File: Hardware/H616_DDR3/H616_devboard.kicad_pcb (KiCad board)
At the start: 8 copper layers, 50 x 50 mm, 169 parts, among them J1 Micro_SD_Card_Det2, J2 HDMI_D_1.4, J3 USB_C_Receptacle_USB2.0, J4 USB_C_Receptacle_USB2.0, J5 Conn_01x40_Pin, Q1 AO3420_C358680, Q2 AO3401A, Q3 AO3401A, SW1 CK_KMS2xxG, U1 H616, U10 D3V3XA4B10LP, U11 D3V3XA4B10LP, U2 K4B8G1646D, U3 AXP305, U4 SW6206, U6 KLMBG2JETD-B041, U7 AP6256, U8 D3V3XA4B10LP, U9 D3V3XA4B10LP, Y1 24MHz

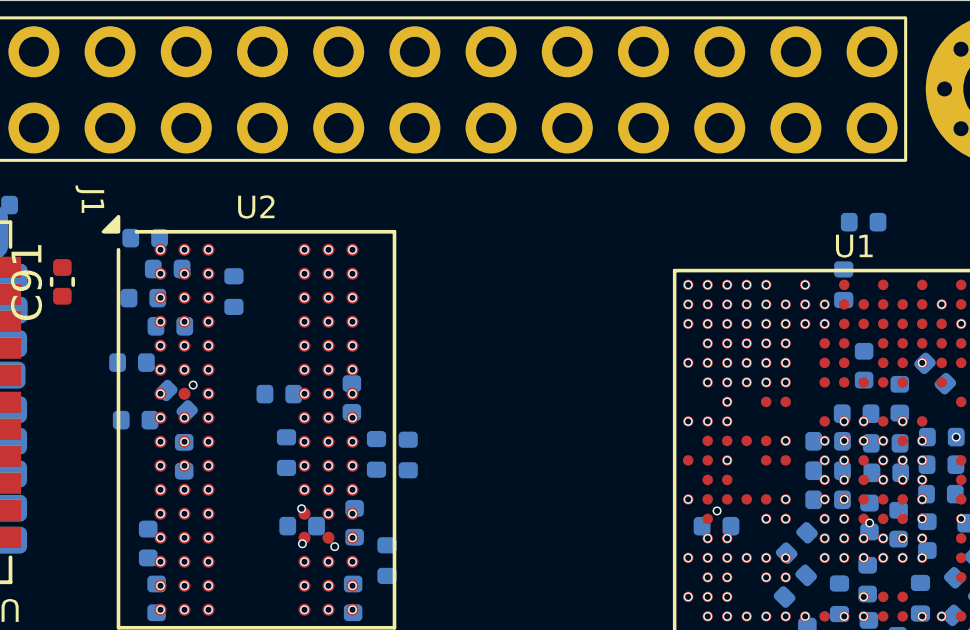
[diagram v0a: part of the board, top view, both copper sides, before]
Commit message: ddr3 trace
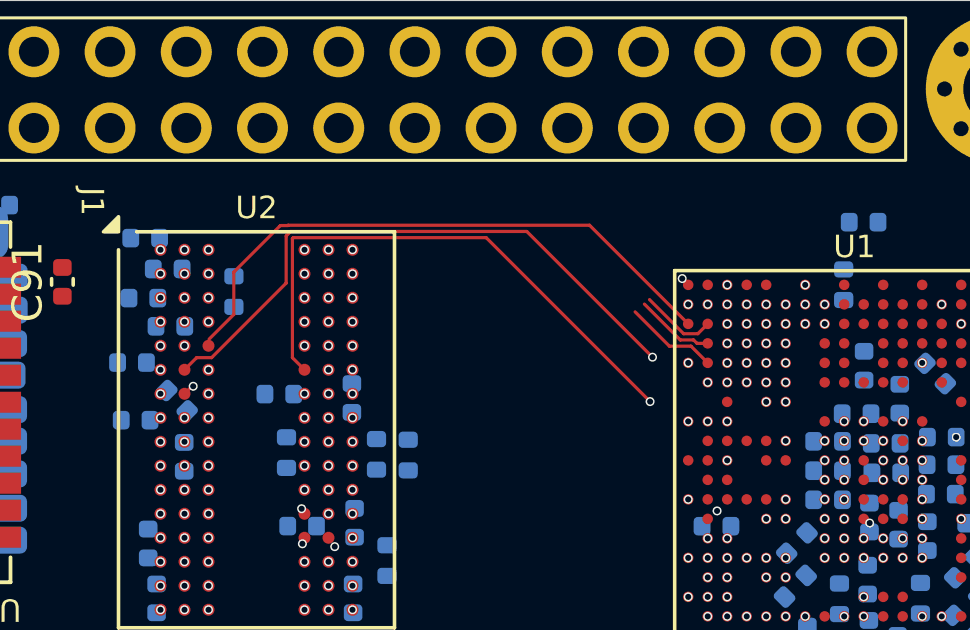
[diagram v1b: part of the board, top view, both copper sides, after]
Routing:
- net /DRAM/DQ1: track 0.00 -> 24.1 mm
- net /DRAM/DQ2: track 0.00 -> 20.2 mm
- net /DRAM/DQ0: track 0.00 -> 19.7 mm, vias 2 -> 0
- net /DRAM/SDQ21: track 0.00 -> 3.12 mm, vias 1 -> 0
- net /DRAM/SDQS1P: track 0.00 -> 2.92 mm
- net /DRAM/DQ10: track 0.00 -> 2.65 mm, vias 2 -> 1
- net /DRAM/DQ14: track 0.00 -> 2.55 mm, vias 2 -> 1
- net /DRAM/SDQS1N: track 0.00 -> 2.29 mm
- net /DRAM/DQ6: track 0.00 -> 0.39 mm, vias 1 -> 2
- net /DRAM/SDQ25: vias 0 -> 1
- net GND: vias 85 -> 84
- net /DRAM/SDQS0N: vias 2 -> 1
- net /DRAM/SDQM0: vias 2 -> 1
- net /DRAM/SDQ26: vias 0 -> 1
- net /DRAM/SDQ22: vias 1 -> 0
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
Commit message: ddr3 trace
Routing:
- removed copper zone on In3.Cu, net /POWER/VDD_CPU
- removed copper zone on In3.Cu, net /POWER/VDD_GPU
- removed copper zone on In1.Cu, net GND
- removed copper zone on In4.Cu, net GND
- removed copper zone on In6.Cu, net GND
- removed copper zone on In3.Cu, net VCC_DRAM
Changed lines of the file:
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@@
 		(net "Net-(U2-ZQ1)")
-	)
-	(zone
-		(net "GND")
-		(layers "In1.Cu" "In4.Cu" "In6.Cu")
-		(name "gnd_1")
-		(hatch edge 0.5)
-		(connect_pads yes
-			(clearance 0.254)
-		)
-		(min_thickness 0.25)
-		(fill yes
-			(thermal_gap 0.5)
-			(thermal_bridge_width 0.5)
-			(island_removal_mode 0)
-		)
-		(polygon
-			(pts
-				(xy 65.2 38.7) (xy 134.075 38.7) (xy 134.075 94.75) (xy 128.95 99.875) (xy 68.875 99.875) (xy 68.875 100)
-				(xy 65.2 96.325)
-			)
-		)
-	)
-	(zone
-		(net "/POWER/VDD_GPU")
-		(layer "In3.Cu")
-		(name "GPU")
-		(hatch edge 0.5)
-		(priority 2)
-		(connect_pads yes
-			(clearance 0.08)
-		)
-		(min_thickness 0.1)
-		(fill yes
-			(thermal_gap 0.5)
-			(thermal_bridge_width 0.5)
-			(smoothing fillet)
-			(radius 1)
-			(island_removal_mode 0)
-		)
-		(polygon
-			(pts
-				(xy 92.43 66.52) (xy 91.01 60.27) (xy 86.9 60.25) (xy 87.53 71.83) (xy 94.48 73.05) (xy 96.676125 77.316131)
-				(xy 106.537905 81.022909) (xy 107.441923 79.49738) (xy 110.264656 79.49199) (xy 110.69 77.55) (xy 107.881031 77.484421)
-				(xy 105.040094 70.498346) (xy 98.53202 68.529472) (xy 95.851615 69.229579) (xy 93.156219 68.375893)
-			)
-		)
-	)
-	(zone
-		(net "VCC_DRAM")
-		(layer "In3.Cu")
-		(name "DRAM")
-		(hatch edge 0.5)
-		(priority 1)
-		(connect_pads yes
-			(clearance 0.15)
-		)
-		(min_thickness 0.25)
-		(fill yes
-			(thermal_gap 0.5)
-			(thermal_bridge_width 0.5)
-			(smoothing fillet)
-			(radius 1)
-			(island_removal_mode 0)
-		)
-		(polygon
-			(pts
-				(xy 98.275 53.325) (xy 115.775 53.325) (xy 116.875 54.425) (xy 116.875 61.850274) (xy 112.73 63.05)
-				(xy 109.116 75.321741) (xy 107.478669 76.091362) (xy 106.77 73.8) (xy 106.860142 70.304477) (xy 104.55419 69.012348)
-				(xy 98.8 68.06) (xy 96.016184 69.03589) (xy 93.720997 68.343259) (xy 92.76 65.11) (xy 99.956046 62.221485)
-				(xy 101.025 56.075)
-			)
-		)
-	)
-	(zone
-		(net "/POWER/VDD_CPU")
-		(layer "In3.Cu")
-		(name "CPU")
-		(hatch edge 0.5)
-		(priority 3)
-		(connect_pads yes
-			(clearance 0.08)
-		)
-		(min_thickness 0.1)
-		(fill yes
-			(thermal_gap 0.5)
-			(thermal_bridge_width 0.5)
-			(smoothing fillet)
-			(radius 1)
-			(island_removal_mode 0)
-		)
-		(polygon
-			(pts
-				(xy 108.84 75.75) (xy 109.5 74.99) (xy 110.1 73.09) (xy 114.48 73.93) (xy 116.684808 80.456232)
-				(xy 114.977772 85.056811) (xy 105.18 85.69) (xy 91.21 83.96) (xy 82.1 77.4) (xy 77.31 69.73) (xy 78.5 55.79)
-				(xy 80.9 53.39) (xy 93.05 53.02) (xy 93.21 57.29) (xy 91.53 59.45) (xy 86.35 59.92) (xy 86.65 72.42)
-				(xy 93.99 73.57) (xy 96.08 77.71) (xy 106.08 81.23) (xy 107.53 80.7) (xy 111.1 80.28) (xy 110.54 77.56)
-				(xy 107.98 77.32) (xy 107.53 75.89)
-			)
-		)
 	)
 	(embedded_fonts no)

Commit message: ddr3 trace
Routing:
- net /DRAM/SDQ21: track 3.12 -> 4.34 mm
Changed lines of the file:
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@@
 	)
 	(segment
-		(start 105.993 54.473)
+		(start 105.01 53.49)
+		(end 104.49 53.49)
+		(width 0.1072)
+		(layer "F.Cu")
+		(net "/DRAM/SDQ21")
+	)
+	(segment
+		(start 105.01 53.49)
 		(end 104.85 53.33)
 		(width 0.1072)
@@
 		(width 0.1072)
 		(layer "F.Cu")
+		(net "/DRAM/SDQ21")
+	)
+	(segment
+		(start 104.49 53.49)
+		(end 104 53)
+		(width 0.1072)
+		(layer "F.Cu")
+		(net "/DRAM/SDQ21")
+	)
+	(segment
+		(start 105.993 54.473)
+		(end 105.01 53.49)
+		(width 0.1072)
+		(layer "F.Cu")

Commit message: pcb
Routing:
- net VCC_DRAM: track 0.00 -> 1.93 mm
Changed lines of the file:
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@@
 		(net "/IO1/SDC0_D2")
+	)
+	(segment
+		(start 96.14 56.86)
+		(end 97 56)
+		(width 0.1)
+		(layer "F.Cu")
+		(net "VCC_DRAM")
+	)
+	(segment
+		(start 95.43 56.86)
+		(end 96.14 56.86)
+		(width 0.1)
+		(layer "F.Cu")
+		(net "VCC_DRAM")
 	)
 	(via

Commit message: pcb
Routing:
- net /DRAM/DQ9: track 0.00 -> 22.0 mm
- net /DRAM/SDQM0: track 0.00 -> 19.4 mm, vias 1 -> 2
- net /DRAM/SDQS0P: track 0.00 -> 17.6 mm
- net /DRAM/SDQS0N: track 0.00 -> 17.2 mm, vias 1 -> 2
- net /DRAM/DQ12: track 0.00 -> 15.7 mm
- net /DRAM/DQ10: track 2.65 -> 16.0 mm
- net /DRAM/SDQ21: track 4.34 -> 0.00 mm
- net /DRAM/SDQS1P: track 2.92 -> 0.00 mm, vias 2 -> 1
- net /DRAM/SDQS1N: track 2.29 -> 0.00 mm, vias 2 -> 1
- net VCC_DRAM: track 1.93 -> 0.67 mm
- net GND: track 1.34 -> 2.07 mm

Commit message: pcb
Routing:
- net /DRAM/DQ11: track 0.00 -> 25.1 mm
- net /DRAM/SDQS1P: track 0.00 -> 23.1 mm, vias 1 -> 2
- net /DRAM/SDQS1N: track 0.00 -> 22.4 mm, vias 1 -> 2
- net /DRAM/DQ15: track 0.00 -> 22.3 mm
- net /DRAM/DQ8: track 0.00 -> 15.0 mm, vias 2 -> 0
- net /DRAM/DQ10: track 16.0 -> 13.7 mm
- net /DRAM/DQ2: track 20.2 -> 22.3 mm
- net /DRAM/DQ0: track 20.1 -> 21.8 mm
- net /DRAM/SDQM0: track 19.4 -> 20.7 mm
- net /DRAM/DQ9: track 22.0 -> 23.2 mm
- net /DRAM/DQ1: track 24.1 -> 24.8 mm

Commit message: ddr trace
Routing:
- net /DRAM/DQ6: track 0.39 -> 27.5 mm
- net /DRAM/DQ13: track 0.00 -> 23.9 mm
- net /DRAM/DQ4: track 0.00 -> 22.7 mm
- net /DRAM/DQ7: track 0.00 -> 20.0 mm
- net /DRAM/SDQM1: track 0.00 -> 16.0 mm
- net /DRAM/DQ5: track 0.00 -> 15.4 mm
- net /DRAM/DQ3: track 0.00 -> 14.9 mm, vias 2 -> 1
- net /DRAM/DQ14: track 2.55 -> 13.7 mm, vias 1 -> 0
- net /DRAM/DQ2: track 22.3 -> 26.6 mm
- net /DRAM/DQ15: track 22.3 -> 25.6 mm
- net /DRAM/DQ11: track 25.1 -> 26.3 mm
- net GND: track 2.07 -> 2.69 mm
- net /IO1/SDC0_D3: vias 1 -> 0
- net /IO1/SDC0_D2: vias 1 -> 0
- net /DRAM/SDQS2P: vias 1 -> 0
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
